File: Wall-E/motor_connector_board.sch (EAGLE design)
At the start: 19 parts, among them U1 JST_SH_4, U2 JST_SH_6, U3 JST_SH_6, U4 MOLEX_ULTRAFIT, U5 SMC

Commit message: completed first motor pcb
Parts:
- added TP1, TP10, TP11, TP2, TP3, TP4, TP5, TP6, TP7, TP8, TP9: TEST-POINT3X4, SparkFun-Connectors:TEST-POINT3X4
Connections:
- net ACS_GND: now also TP4.1
- net ACS_OUT: now also TP5.1
- net ENC_A: now also TP6.1
- net ENC_B: now also TP7.1
- net ENC_GND: now also TP9.1
- net ENC_VCC: now also TP8.1
- net GND: now also TP1.1, TP2.1
- net MOTORA: now also TP10.1
- net MOTORB: now also TP11.1
- net SMC_ERR: now also TP3.1
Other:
- note added: "Test Points"
- moved on the sheet: C2, J10, J12, J2, R1, R2, R3, R4, U$1, U1, U2, U3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

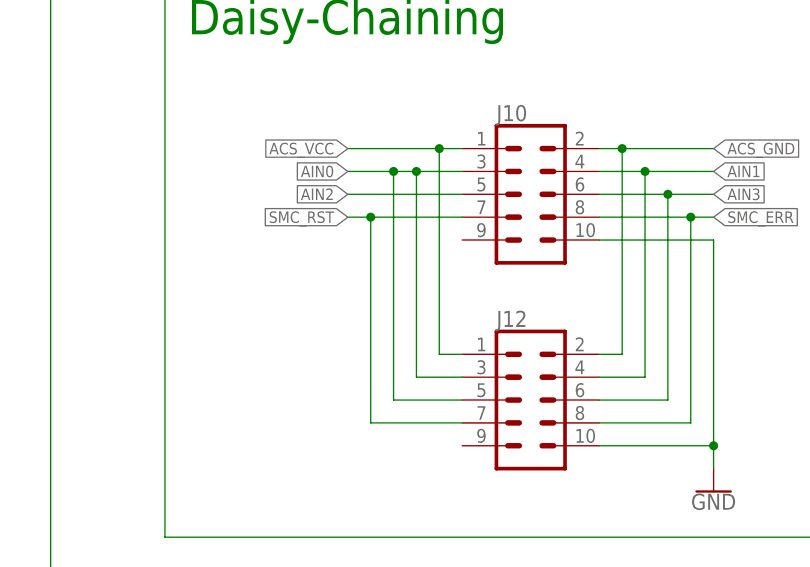
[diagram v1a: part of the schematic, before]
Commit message: fixed error on ribbon cable connector
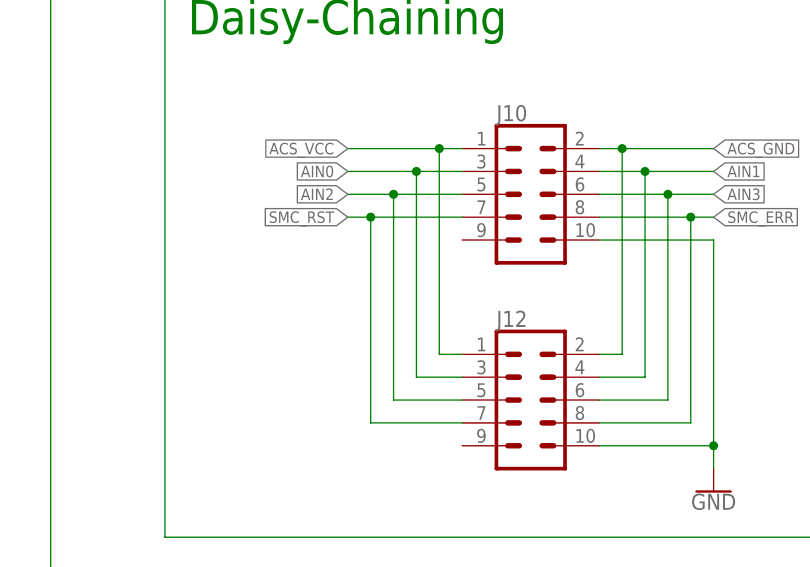
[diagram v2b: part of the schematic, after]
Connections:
- net AIN0: no longer J12.5
- net AIN2: now also J12.5
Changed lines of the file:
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@@
 <segment>
 <pinref part="J10" gate="G$1" pin="5"/>
-<wire x1="251.46" y1="50.8" x2="238.76" y2="50.8" width="0.1524" layer="91"/>
+<wire x1="251.46" y1="50.8" x2="243.84" y2="50.8" width="0.1524" layer="91"/>
 <label x="238.76" y="50.8" size="1.27" layer="95" rot="R180" xref="yes"/>
+<pinref part="J12" gate="G$1" pin="5"/>
+<wire x1="243.84" y1="50.8" x2="238.76" y2="50.8" width="0.1524" layer="91"/>
+<wire x1="251.46" y1="27.94" x2="243.84" y2="27.94" width="0.1524" layer="91"/>
+<wire x1="243.84" y1="27.94" x2="243.84" y2="50.8" width="0.1524" layer="91"/>
+<junction x="243.84" y="50.8"/>
 </segment>
 </net>
@@
 <wire x1="251.46" y1="53.34" x2="246.38" y2="53.34" width="0.1524" layer="91"/>
 <pinref part="J12" gate="G$1" pin="3"/>
-<wire x1="246.38" y1="53.34" x2="243.84" y2="53.34" width="0.1524" layer="91"/>
-<wire x1="243.84" y1="53.34" x2="238.76" y2="53.34" width="0.1524" layer="91"/>
+<wire x1="246.38" y1="53.34" x2="238.76" y2="53.34" width="0.1524" layer="91"/>
 <wire x1="251.46" y1="30.48" x2="246.38" y2="30.48" width="0.1524" layer="91"/>
 <wire x1="246.38" y1="30.48" x2="246.38" y2="53.34" width="0.1524" layer="91"/>
 <junction x="246.38" y="53.34"/>
-<pinref part="J12" gate="G$1" pin="5"/>
-<wire x1="251.46" y1="27.94" x2="243.84" y2="27.94" width="0.1524" layer="91"/>
-<wire x1="243.84" y1="27.94" x2="243.84" y2="53.34" width="0.1524" layer="91"/>
-<junction x="243.84" y="53.34"/>
 <label x="238.76" y="53.34" size="1.27" layer="95" rot="R180" xref="yes"/>
 </segment>

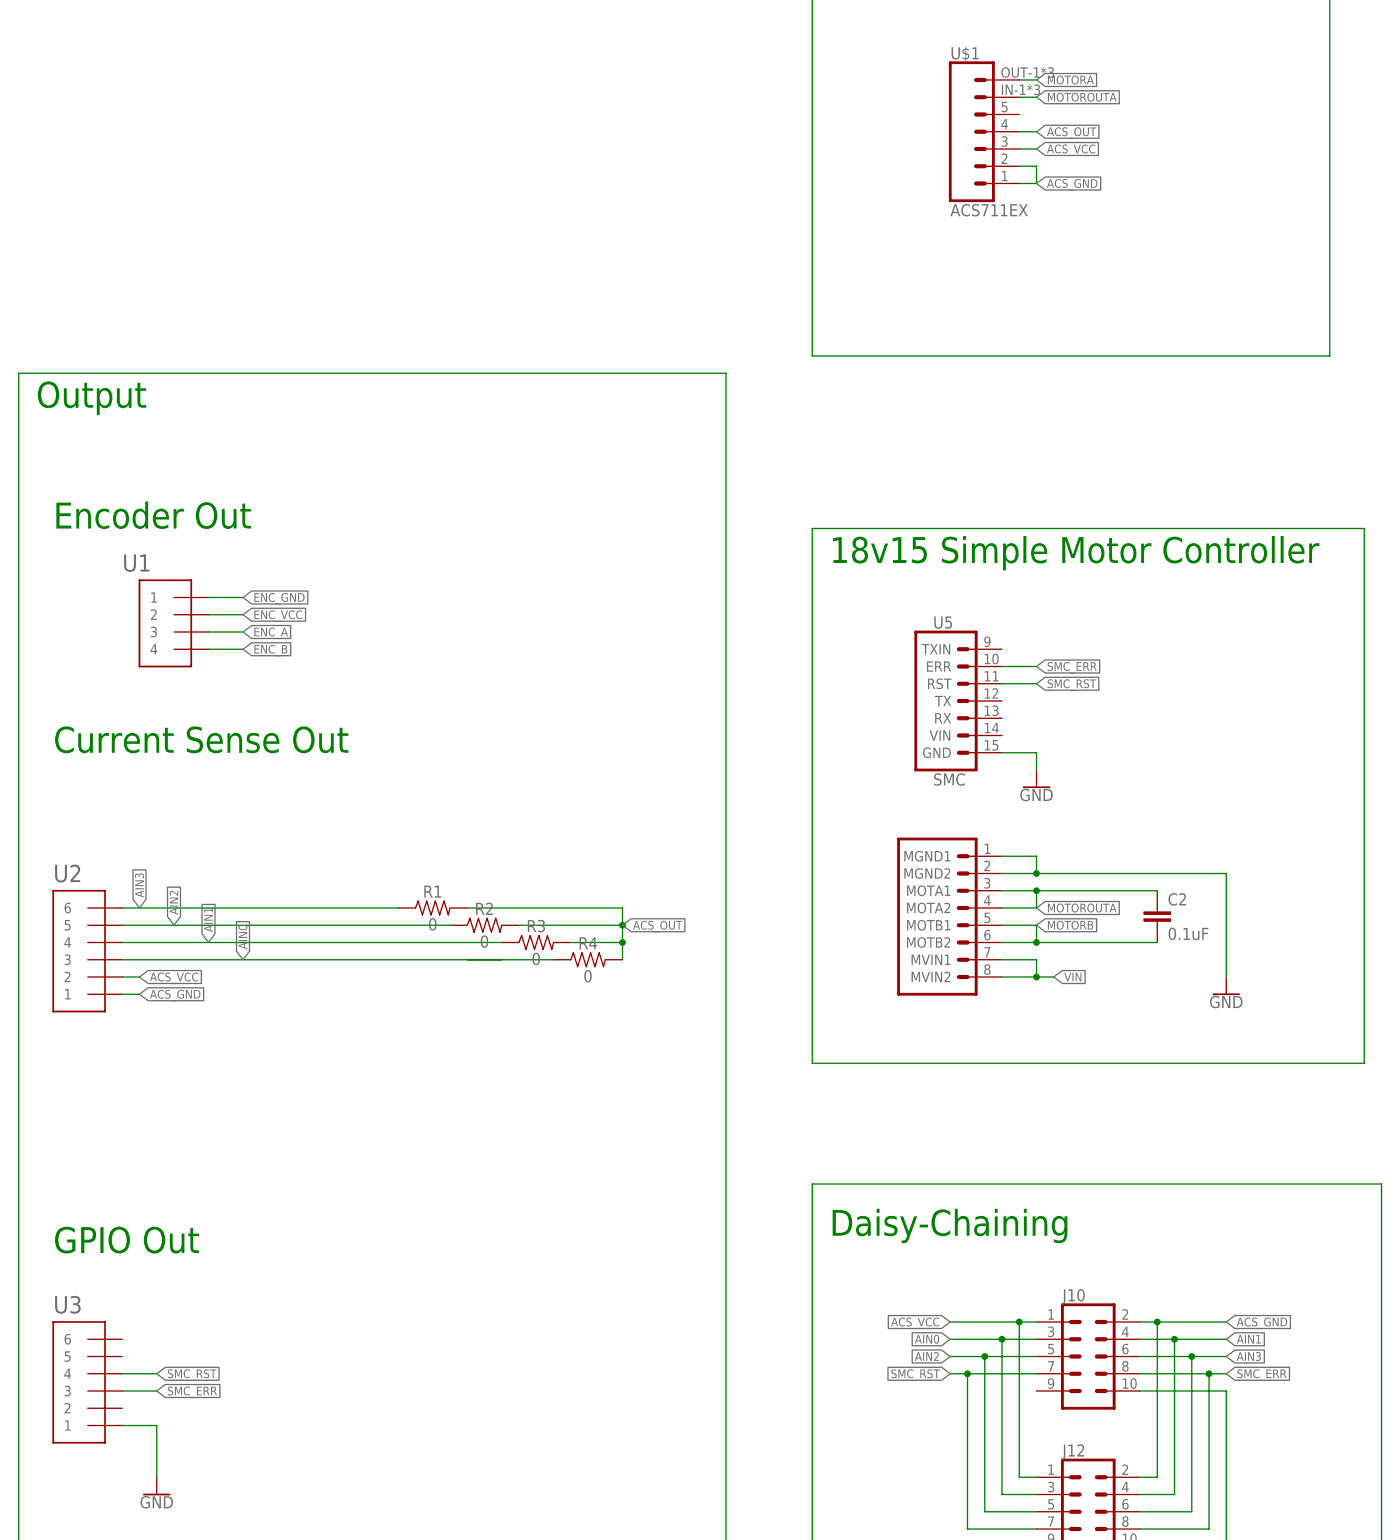
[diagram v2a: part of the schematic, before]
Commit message: added voltage divider for current sense, rerouted current sense power to a 3.3 line, and minor tweaks to routing
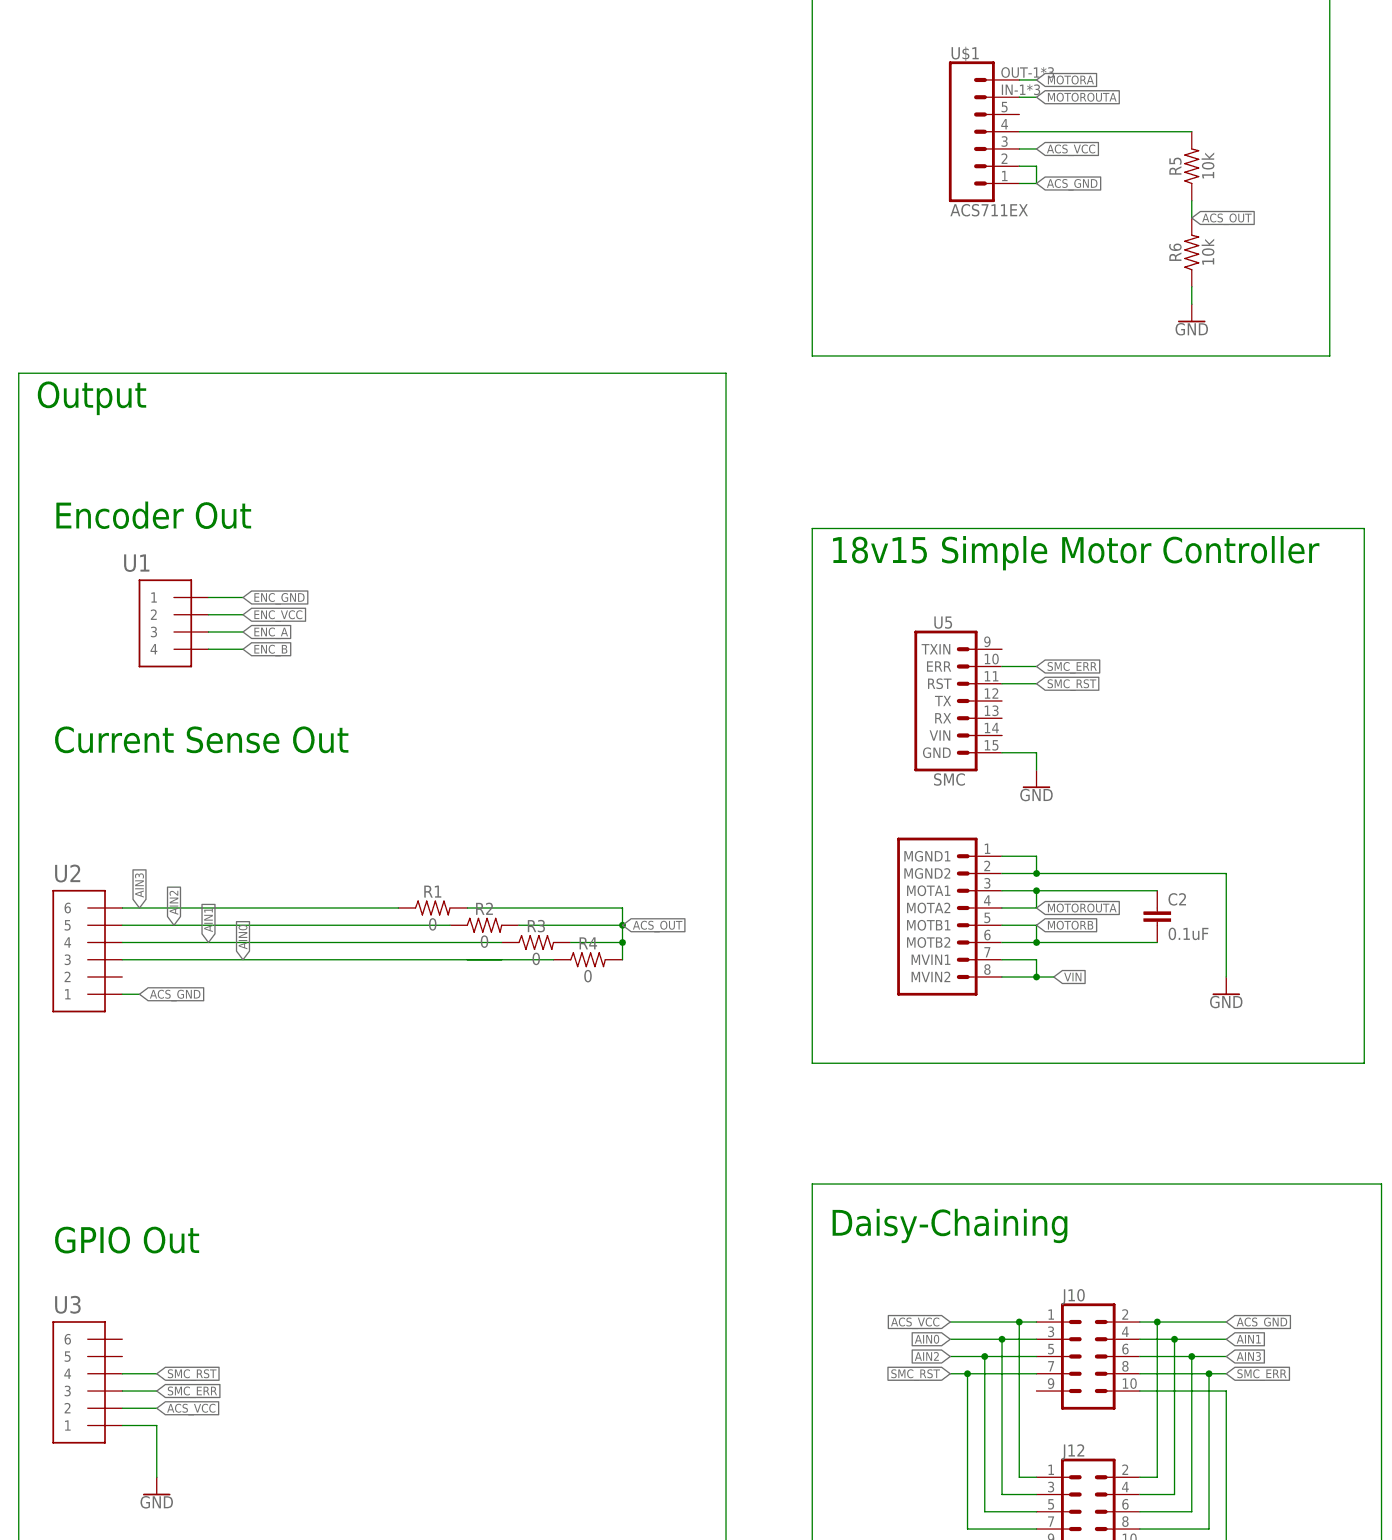
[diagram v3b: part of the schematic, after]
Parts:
- added R5, R6: 10k, SparkFun-Resistors:10KOHM-0603-1/10W-1%
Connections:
- new net ACS_3.3OUT: R5.2, U$1.4
- net ACS_OUT: now also R5.1, R6.2; no longer U$1.4
- net ACS_VCC: now also U3.2; no longer U2.2
- net GND: now also R6.1
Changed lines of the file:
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@@
 <part name="TP10" library="SparkFun-Connectors" deviceset="TEST-POINT" device="3X4"/>
 <part name="TP11" library="SparkFun-Connectors" deviceset="TEST-POINT" device="3X4"/>
+<part name="R5" library="SparkFun-Resistors" deviceset="10KOHM" device="-0603-1/10W-1%" value="10k"/>
+<part name="R6" library="SparkFun-Resistors" deviceset="10KOHM" device="-0603-1/10W-1%" value="10k"/>
+<part name="GND5" library="SparkFun-PowerSymbols" deviceset="GND" device=""/>
 </parts>
 <sheets>
@@
 <instance part="TP10" gate="G$1" x="355.6" y="111.76"/>
 <instance part="TP11" gate="G$1" x="355.6" y="104.14"/>
+<instance part="R5" gate="G$1" x="274.32" y="226.06" rot="R90"/>
+<instance part="R6" gate="G$1" x="274.32" y="213.36" rot="R90"/>
+<instance part="GND5" gate="1" x="274.32" y="203.2"/>
 </instances>
 <busses>
@@
 <wire x1="350.52" y1="175.26" x2="350.52" y2="182.88" width="0.1524" layer="91"/>
 <label x="347.98" y="180.34" size="1.27" layer="95" rot="R180" xref="yes"/>
+</segment>
+<segment>
+<pinref part="R6" gate="G$1" pin="1"/>
+<pinref part="GND5" gate="1" pin="GND"/>
+<wire x1="274.32" y1="205.74" x2="274.32" y2="208.28" width="0.1524" layer="91"/>
 </segment>
 </net>
@@
 </segment>
 <segment>
-<pinref part="U$1" gate="G$1" pin="4"/>
-<wire x1="248.92" y1="231.14" x2="251.46" y2="231.14" width="0.1524" layer="91"/>
-<label x="251.46" y="231.14" size="1.27" layer="95" xref="yes"/>
-</segment>
-<segment>
 <pinref part="TP5" gate="G$1" pin="1"/>
 <wire x1="355.6" y1="152.4" x2="350.52" y2="152.4" width="0.1524" layer="91"/>
 <label x="350.52" y="152.4" size="1.27" layer="95" rot="R180" xref="yes"/>
 </segment>
+<segment>
+<pinref part="R6" gate="G$1" pin="2"/>
+<pinref part="R5" gate="G$1" pin="1"/>
+<wire x1="274.32" y1="218.44" x2="274.32" y2="220.98" width="0.1524" layer="91"/>
+<label x="274.32" y="218.44" size="1.27" layer="95" xref="yes"/>
+</segment>
 </net>
 <net name="ACS_VCC" class="0">
-<segment>
-<pinref part="U2" gate="G$1" pin="2"/>
-<wire x1="116.84" y1="106.68" x2="119.38" y2="106.68" width="0.1524" layer="91"/>
-<label x="119.38" y="106.68" size="1.27" layer="95" xref="yes"/>
-</segment>
 <segment>
 <pinref part="J10" gate="G$1" pin="1"/>
@@
 <label x="251.46" y="228.6" size="1.27" layer="95" xref="yes"/>
 </segment>
+<segment>
+<pinref part="U3" gate="G$1" pin="2"/>
+<wire x1="116.84" y1="43.18" x2="121.92" y2="43.18" width="0.1524" layer="91"/>
+<label x="121.92" y="43.18" size="1.27" layer="95" xref="yes"/>
+</segment>
 </net>
 <net name="ACS_GND" class="0">
@@
 </segment>
 </net>
+<net name="ACS_3.3OUT" class="0">
+<segment>
+<pinref part="U$1" gate="G$1" pin="4"/>
+<pinref part="R5" gate="G$1" pin="2"/>
+<wire x1="274.32" y1="231.14" x2="248.92" y2="231.14" width="0.1524" layer="91"/>
+</segment>
+</net>
